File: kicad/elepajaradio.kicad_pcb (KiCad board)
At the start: 2 copper layers, 44 x 47 mm, 29 parts, among them J1 SPI, J2 UART, J3 vdd_gnd, J4 reset, J5 OLED, SW1 RotaryEncoder, SW2 SW_Push, SW3 SW_Push, U1 MAX2606, U3 ATmega328PB-A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

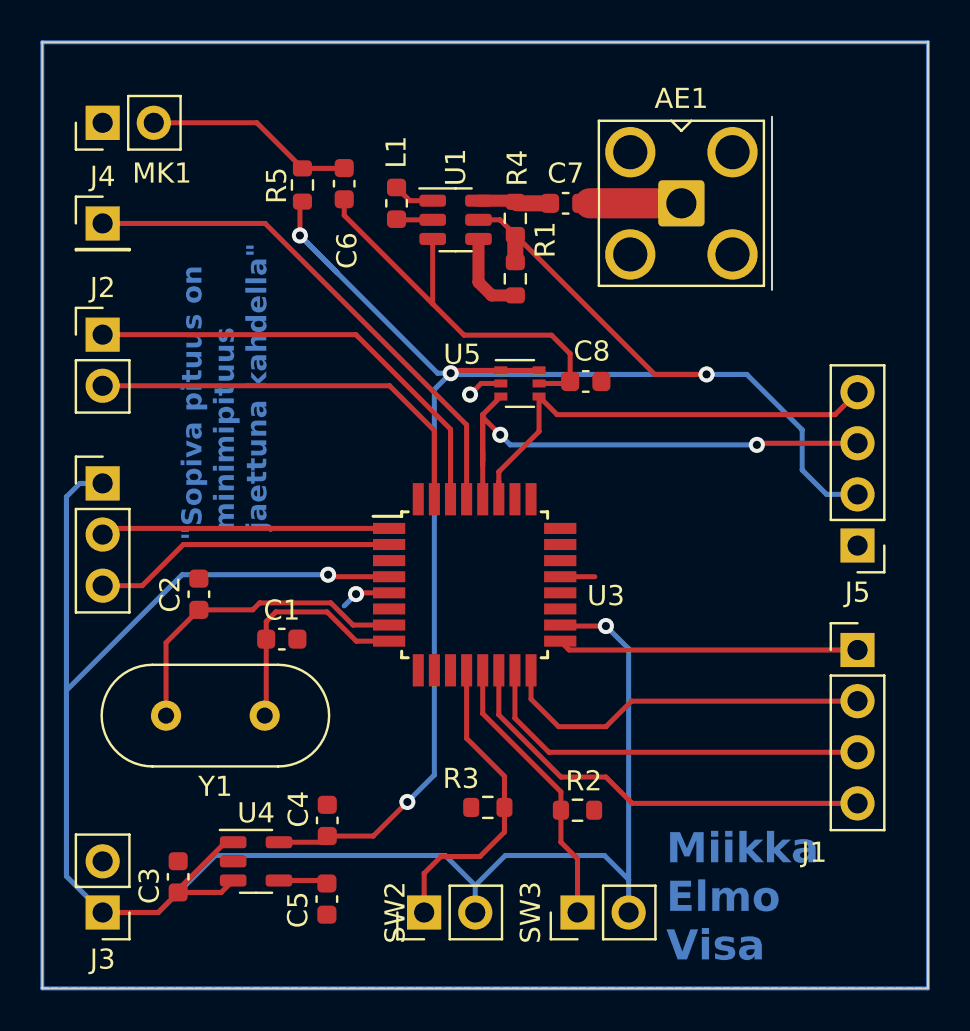
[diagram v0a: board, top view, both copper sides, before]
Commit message: pull-up resistors and diode added
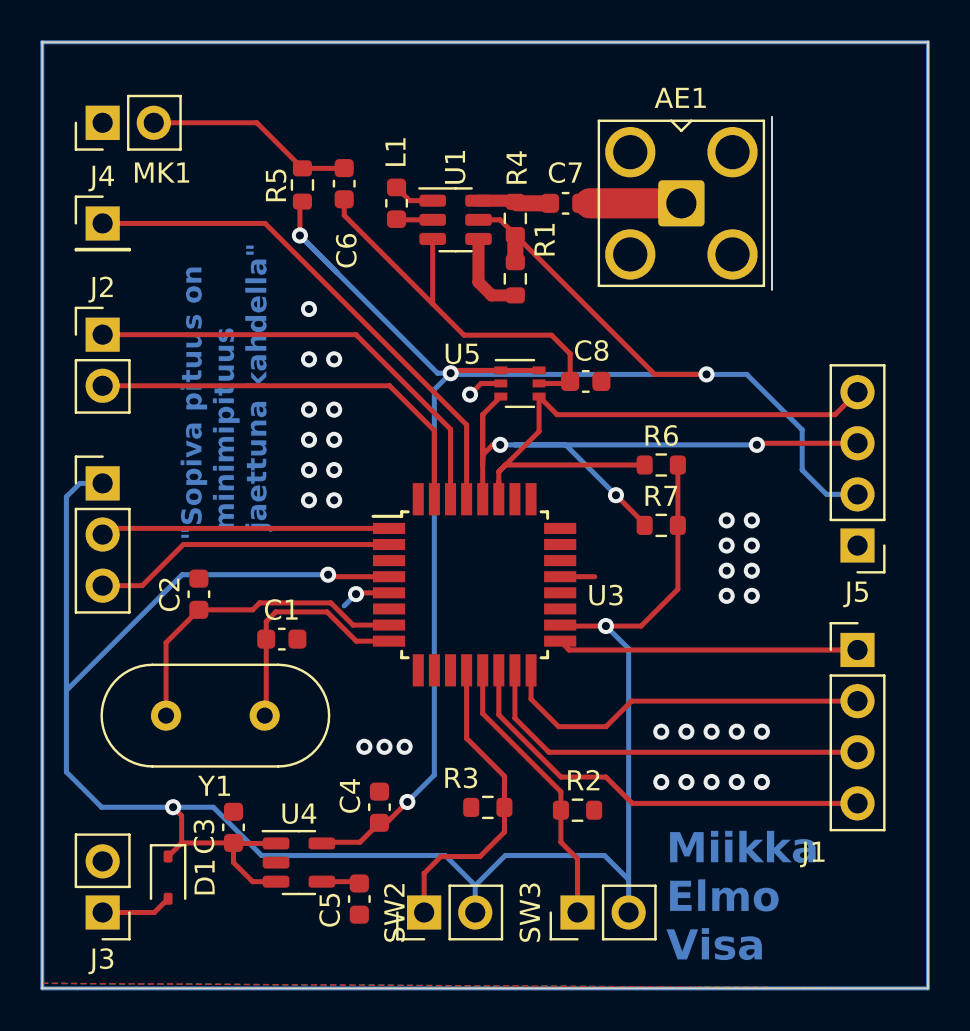
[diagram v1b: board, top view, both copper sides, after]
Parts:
- added D1: 1N4148WS, Diode_SMD:D_SOD-323, F.Cu at (128.2, 112.5)
- added R6: 4k7, Resistor_SMD:R_0603_1608Metric, F.Cu at (152.8, 92.0)
- added R7: 4k7, Resistor_SMD:R_0603_1608Metric, F.Cu at (152.8, 95.0)
- moved C3 3.69 mm to (131.5, 110.0)
- moved C4 2.67 mm to (138.8, 109.0)
- moved U4 2.13 mm to (134.8, 111.8)
- moved C5 1.61 mm to (137.8, 113.6)
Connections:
- AE1 pad 2: GND -> (no net)
- J3 pad 1: VDD -> Net-(D1-A)
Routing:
- net SCL0: track 27.6 -> 35.3 mm, vias 2 -> 3
- net SDA0: track 23.5 -> 30.9 mm
- net Net-(D1-A): track 0.00 -> 3.53 mm
- net VDD: track 102.1 -> 105.5 mm, vias 2 -> 3
- net 3V3: track 88.7 -> 86.6 mm
- net Net-(U4-ADJ): track 2.44 -> 1.90 mm
- net GND: vias 2 -> 34
